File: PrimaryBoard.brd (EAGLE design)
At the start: 83.8 x 54.6 mm, 29 parts, among them J10 LORA32U4II, J11 CONN_42.54_SCREW, J13 POWER_JACK, J4 CONN_32.54_SCREW, J5 CONN_32.54_SCREW, J6 CONN_32.54_SCREW, J7 CONN_32.54_SCREW, J8 CONN_32.54_SCREW, J9 CONN_32.54_SCREW, U1 CD74HC4052PW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

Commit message: Minor updates and cleanup for primary board
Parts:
- added R2, R3: 10k, bschulz:R0805
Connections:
- net 3V3_CORE: now also R2.2, R3.2
- net SCL: now also R3.1
- net SDA: now also R2.1
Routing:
- net 3V3_CORE: track 153.4 -> 198.6 mm
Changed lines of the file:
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@@
 <drawing>
 <settings>
-<setting alwaysvectorfont="yes"/>
+<setting alwaysvectorfont="no"/>
 <setting verticaltext="up"/>
 </settings>
@@
 <attribute name="VALUE" x="19.177" y="19.05" size="0.6096" layer="27" font="vector" ratio="15" rot="R90" align="center"/>
 </element>
+<element name="R2" library="bschulz" package="R0805" value="10k" x="72.39" y="8.763" smashed="yes" rot="R90">
+<attribute name="NAME" x="71.12" y="8.128" size="1.27" layer="25" rot="R90"/>
+<attribute name="VALUE" x="74.93" y="8.128" size="1.27" layer="27" rot="R90"/>
+</element>
+<element name="R3" library="bschulz" package="R0805" value="10k" x="74.93" y="8.763" smashed="yes" rot="R90">
+<attribute name="NAME" x="73.66" y="8.128" size="1.27" layer="25" rot="R90"/>
+<attribute name="VALUE" x="77.47" y="8.128" size="1.27" layer="27" rot="R90"/>
+</element>
 </elements>
 <signals>
@@
 <wire x1="37.5196125" y1="35.9158" x2="55.2419875" y2="35.9158" width="0.4064" layer="16"/>
 <wire x1="15.24" y1="29.21" x2="17.145" y2="31.115" width="0.4064" layer="1"/>
+<contactref element="R2" pad="2"/>
+<contactref element="R3" pad="2"/>
+<wire x1="74.93" y1="9.713" x2="72.39" y2="9.713" width="0.254" layer="1"/>
+<wire x1="72.39" y1="9.713" x2="72.39" y2="34.163" width="0.254" layer="1"/>
+<wire x1="62.103" y1="44.45" x2="58.42" y2="44.45" width="0.254" layer="1"/>
+<wire x1="72.39" y1="34.163" x2="62.103" y2="44.45" width="0.254" layer="1"/>
 </signal>
 <signal name="3V3_EXT">
@@
 <wire x1="43.688" y1="8.1788" x2="48.5902" y2="8.1788" width="0.254" layer="1"/>
 <wire x1="48.5902" y1="8.1788" x2="49.657" y2="7.112" width="0.254" layer="1"/>
-<wire x1="49.657" y1="7.112" x2="79.492" y2="7.112" width="0.254" layer="1"/>
-<wire x1="79.492" y1="7.112" x2="81.28" y2="8.9" width="0.254" layer="1"/>
+<contactref element="R2" pad="1"/>
+<wire x1="49.657" y1="7.112" x2="71.689" y2="7.112" width="0.254" layer="1"/>
+<wire x1="71.689" y1="7.112" x2="72.39" y2="7.813" width="0.254" layer="1"/>
+<wire x1="72.39" y1="7.813" x2="73.35" y2="8.773" width="0.254" layer="1"/>
+<wire x1="81.153" y1="8.773" x2="81.28" y2="8.9" width="0.254" layer="1"/>
+<wire x1="81.153" y1="8.773" x2="73.35" y2="8.773" width="0.254" layer="1"/>
 </signal>
 <signal name="SCL">
@@
 <wire x1="43.688" y1="7.5184" x2="48.66173125" y2="7.5184" width="0.254" layer="1"/>
 <wire x1="48.66173125" y1="7.5184" x2="49.59153125" y2="6.5886" width="0.254" layer="1"/>
-<wire x1="80.6296" y1="6.5886" x2="82.55" y2="8.509" width="0.254" layer="1"/>
 <wire x1="82.55" y1="8.509" x2="82.55" y2="10.16" width="0.254" layer="1"/>
 <wire x1="82.55" y1="10.16" x2="81.28" y2="11.43" width="0.254" layer="1"/>
-<wire x1="49.59153125" y1="6.5886" x2="80.6296" y2="6.5886" width="0.254" layer="1"/>
+<contactref element="R3" pad="1"/>
+<wire x1="49.59153125" y1="6.5886" x2="73.7056" y2="6.5886" width="0.254" layer="1"/>
+<wire x1="73.7056" y1="6.5886" x2="74.93" y2="7.813" width="0.254" layer="1"/>
+<wire x1="74.93" y1="7.813" x2="74.9756" y2="7.8586" width="0.254" layer="1"/>
+<wire x1="81.8996" y1="7.8586" x2="74.9756" y2="7.8586" width="0.254" layer="1"/>
+<wire x1="81.8996" y1="7.8586" x2="82.55" y2="8.509" width="0.254" layer="1"/>
 </signal>
 <signal name="ONEWIRE">

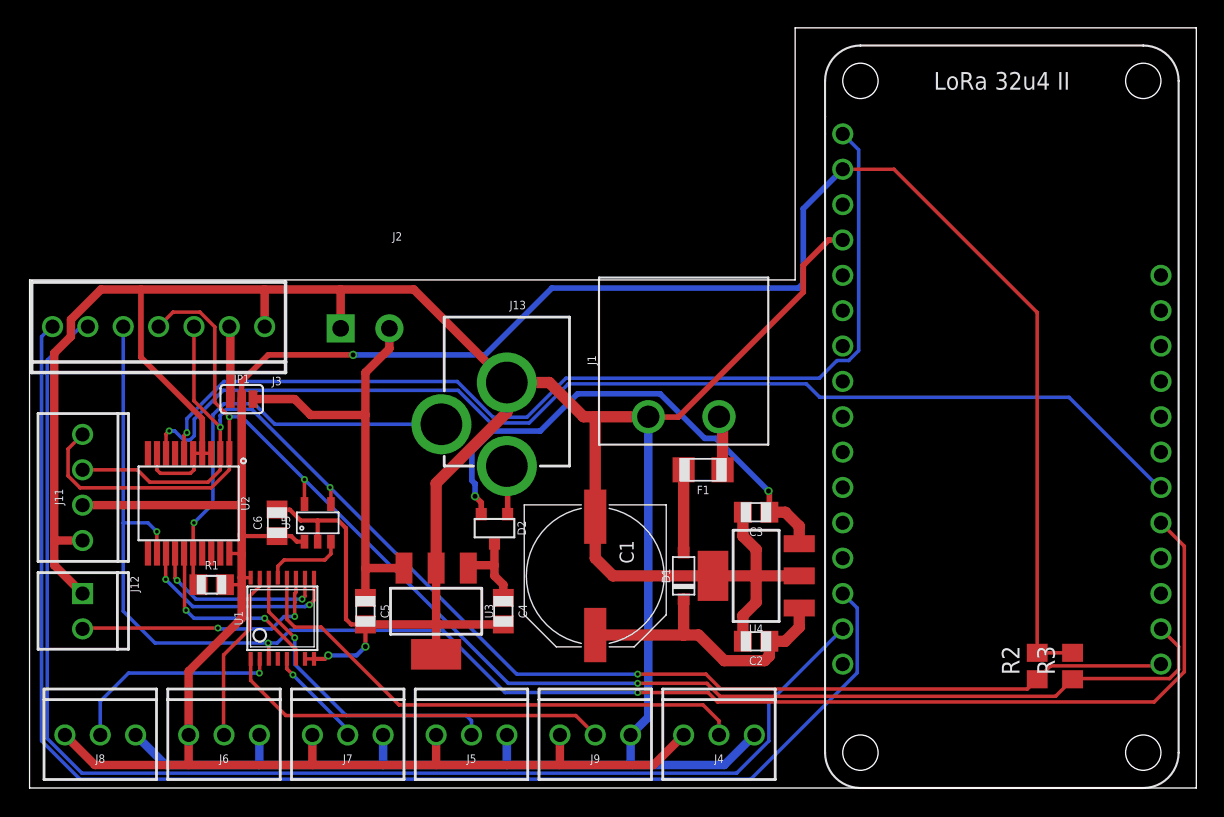
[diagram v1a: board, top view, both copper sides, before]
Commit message: Minor updates to Primary and Remote
Cleaned up/added silkscreen, added test points to both boards
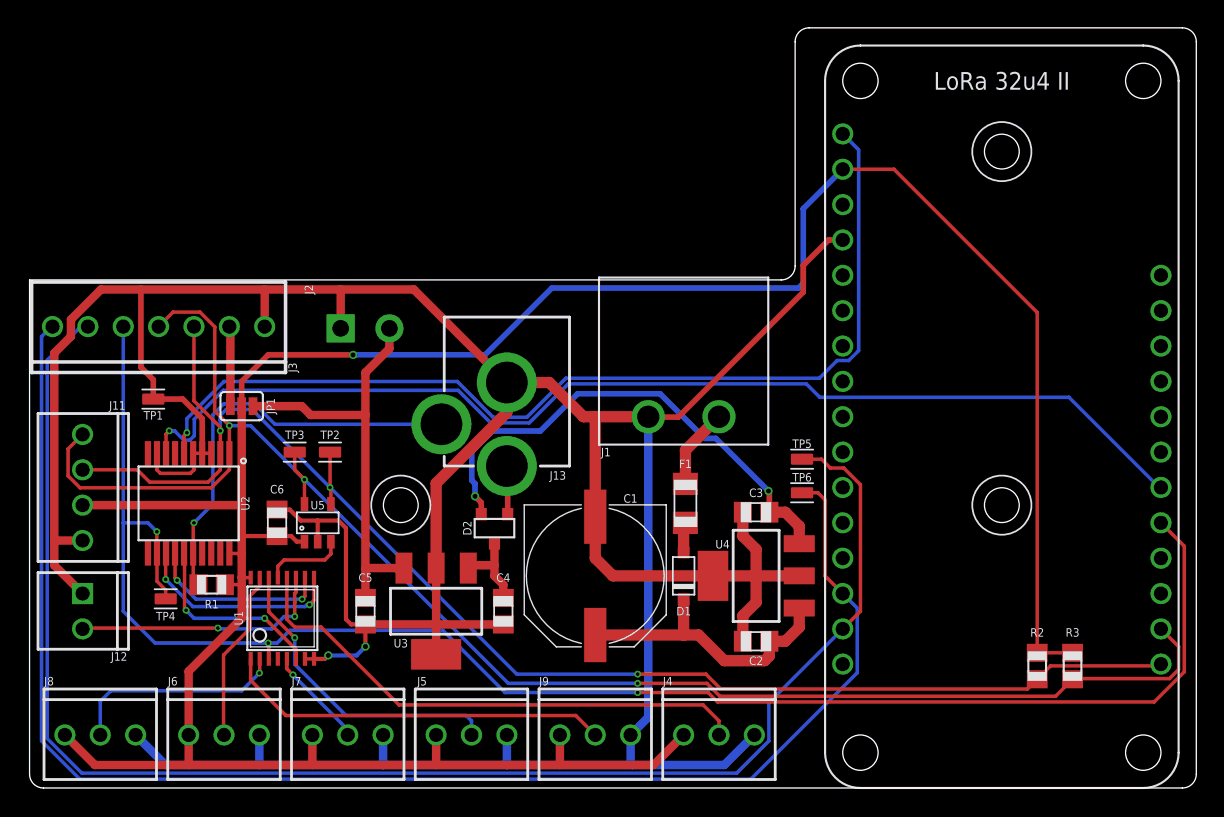
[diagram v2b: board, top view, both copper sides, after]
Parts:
- added H1, H2, H3: (no value), bschulz:2_56
- added TP1, TP2, TP3, TP4, TP5, TP6: TESTPOINTRCU, bschulz:TESTPOINT_0603
- R2, R3: device bschulz:R0805 -> bschulz_passives:R0805
- moved F1 2.73 mm to (47.1, 20.4), turned to 270 degrees
- moved JP1 0.51 mm to (15.2, 27.4)
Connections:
- net GND: now also TP1.1
- net ONEWIRE: now also TP4.1
- net RX: now also TP6.1
- net SCL: now also TP3.1
- net SDA: now also TP2.1
- net TX: now also TP5.1
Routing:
- net TX: track 95.2 -> 111.0 mm
- net RX: track 99.2 -> 108.3 mm
- net N$3: track 5.95 -> 2.18 mm
- net ONEWIRE: track 117.8 -> 121.3 mm
- net SDA: track 100.6 -> 103.4 mm
- net SCL: track 114.0 -> 116.0 mm
- net 24V_AC: track 3.92 -> 5.82 mm
- net GND: track 282.0 -> 283.2 mm
- net 3V3_EXT: track 5.24 -> 5.75 mm
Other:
- outline, holes or cut-outs redrawn
- board text added: "+"
- board text added: "-"
- board text added: "3v3"
- board text added: "3v3 OUT"
- board text added: "5V 0.5A"
- board text added: "9~12V 150mA DC 24V 150mA AC"
- board text added: "A0"
- board text added: "A1"
- board text added: "A2"
- board text added: "A3"
- board text added: "GND"
- board text added: "I2C AUX"
- board text added: "OW"
- board text added: "OW0"
- board text added: "OW1"
- board text added: "OW2"
- board text added: "OWn"
- board text added: "RX"
- board text added: "SCL"
- board text added: "SDA"
- board text added: "TX"

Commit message: Minor cleanup/fixes to boards, generated gerbers
Minor changes to boards, primarily cleanup and generated gerbers for fab, ready for review
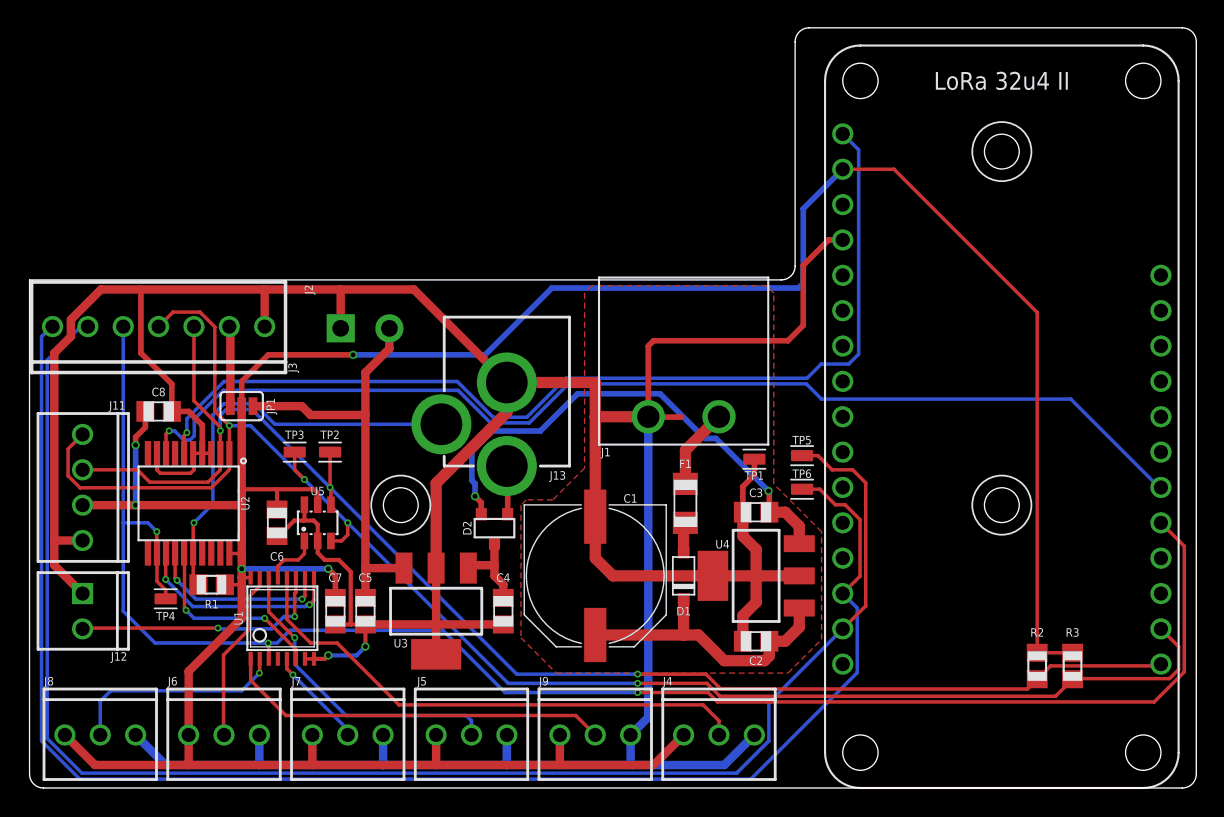
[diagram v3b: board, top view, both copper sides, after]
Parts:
- added C7, C8: 0.1uF, bschulz_passives:C0805
- C6: value (none) -> 0.1uF
- U5: value MCP3221 -> MCP3421A3; device bschulz:SOT23-5 -> bschulz:SOT23-6L
- moved TP1 43.4 mm to (52.1, 23.6)
- moved TP5 0.25 mm to (55.5, 23.9)
- moved TP6 0.25 mm to (55.5, 21.5)
- turned C6 to 270 degrees
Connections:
- net N$1 renamed 5V_CORE
- net N$2 renamed V_RECT
- net 3V3_CORE: now also C7.1, C8.1, U5.5; no longer U5.1
- net A_COM: now also U5.1; no longer U5.3
- net GND: now also C7.2, C8.2, U5.6
- net SCL: now also U5.3; no longer U5.5
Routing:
- net 3V3_CORE: track 198.6 -> 217.5 mm, vias 1 -> 5
- net GND: track 283.2 -> 295.5 mm
- net A_COM: track 5.88 -> 4.03 mm
- net RX: track 108.3 -> 110.0 mm
- net TX: track 111.0 -> 111.7 mm
- net SCL: track 116.0 -> 116.5 mm, vias 3 -> 4
- added copper zone on layer 1, net GND
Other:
- board text added: "Project-Palmer Primary v0.0 Bobby Schulz"

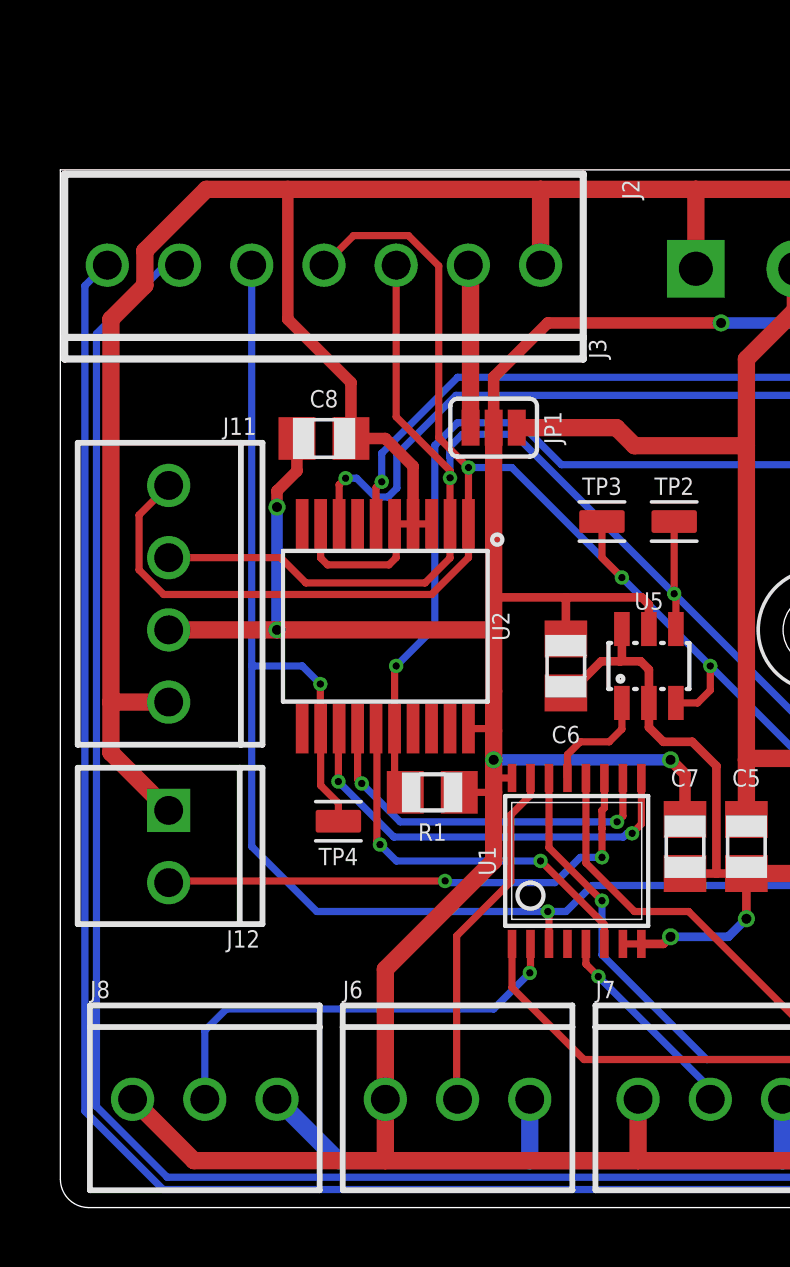
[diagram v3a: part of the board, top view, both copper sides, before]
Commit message: Minor updates, part vals
Changed 1x7 connector on Primary board to 1x4 and 1x3 because 1x7 0.1" screw terminals are made of Corinthian Leather apparently, also updated part values and BoM vals
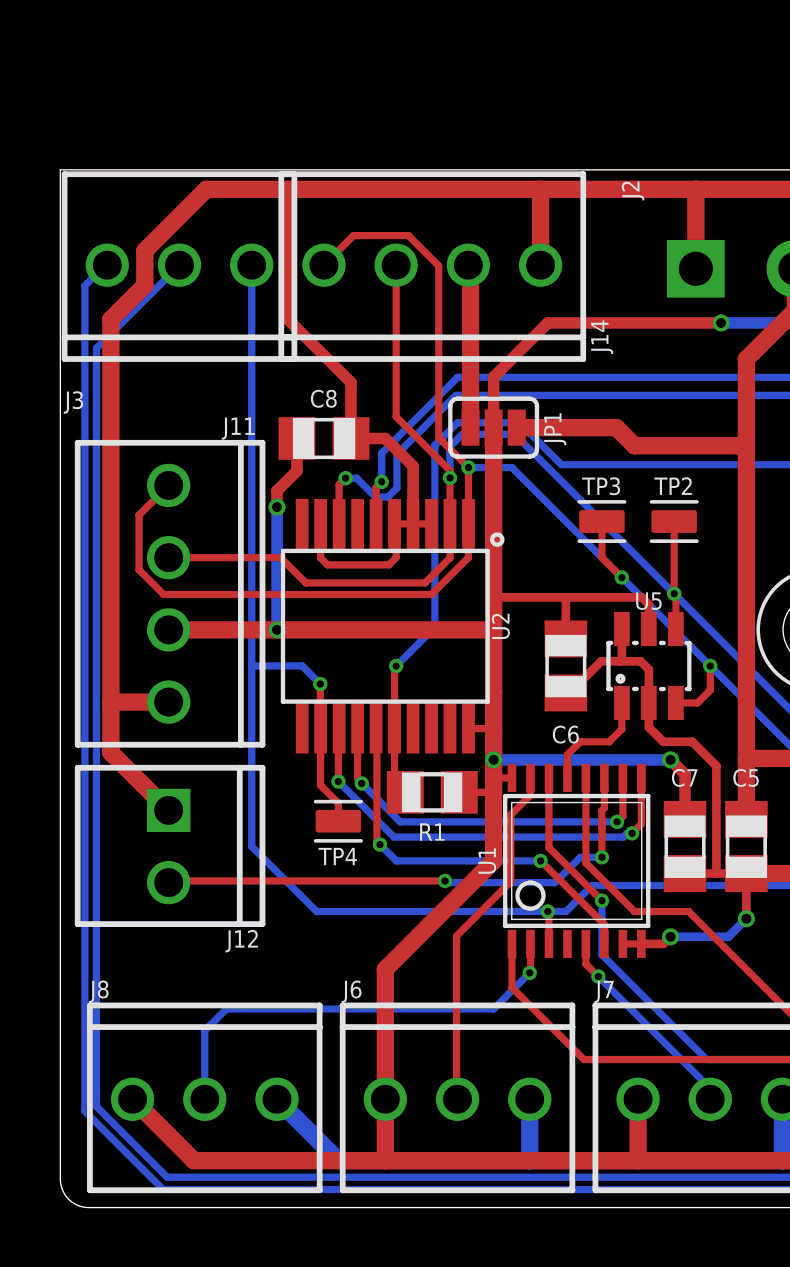
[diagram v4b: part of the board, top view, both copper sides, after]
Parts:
- added J14: CONN_42.54_SCREW, bschulz:1X04_SCREW
- J3: value (none) -> CONN_32.54_SCREW; device bschulz:1X07_SCREW -> bschulz:1X03_SCREW
- moved J3 6.35 mm to (4.19, 33.1), turned to 0 degrees
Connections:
- net 3V3_EXT: now also J14.3; no longer J3.2
- net GND: now also J14.4; no longer J3.1
- net ONEWIRE: now also J3.3; no longer J3.5
- net RX: now also J3.1; no longer J3.7
- net SCL: now also J14.1; no longer J3.4
- net SDA: now also J14.2; no longer J3.3
- net TX: now also J3.2; no longer J3.6
